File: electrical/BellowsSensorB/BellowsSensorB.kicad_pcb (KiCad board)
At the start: 2 copper layers, 32 x 20 mm, 5 parts, among them J1 I2C, U1 WF200DPZ 0.1BG S16 DT

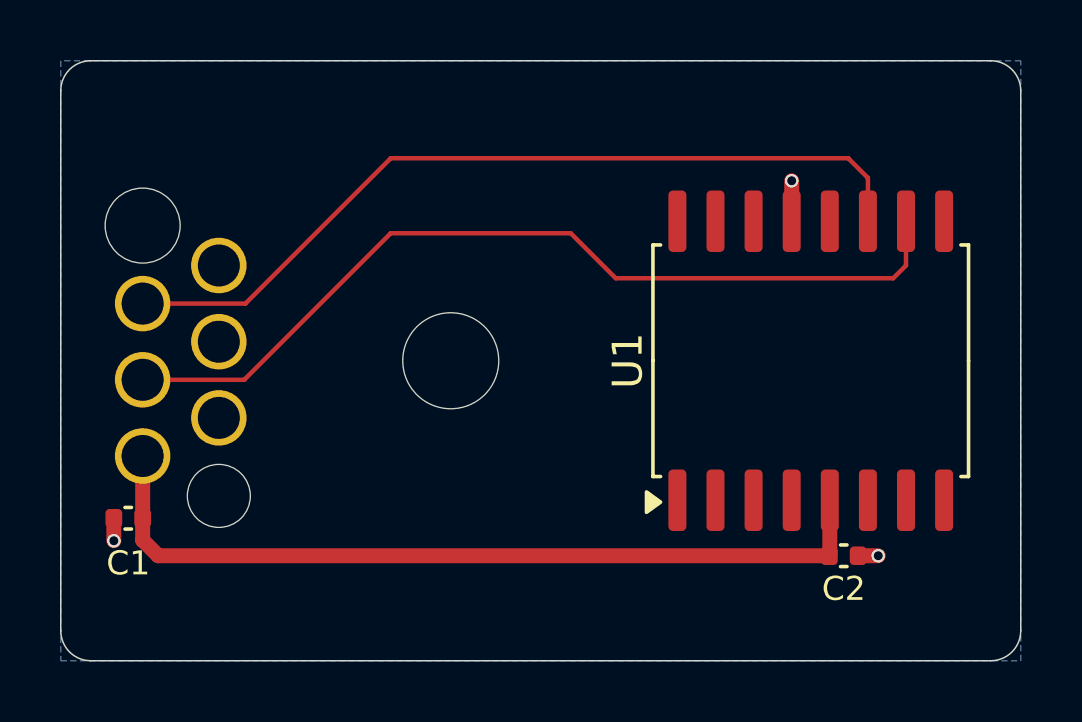
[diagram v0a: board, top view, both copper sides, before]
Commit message: Add solder bridges to BellowsSensorB
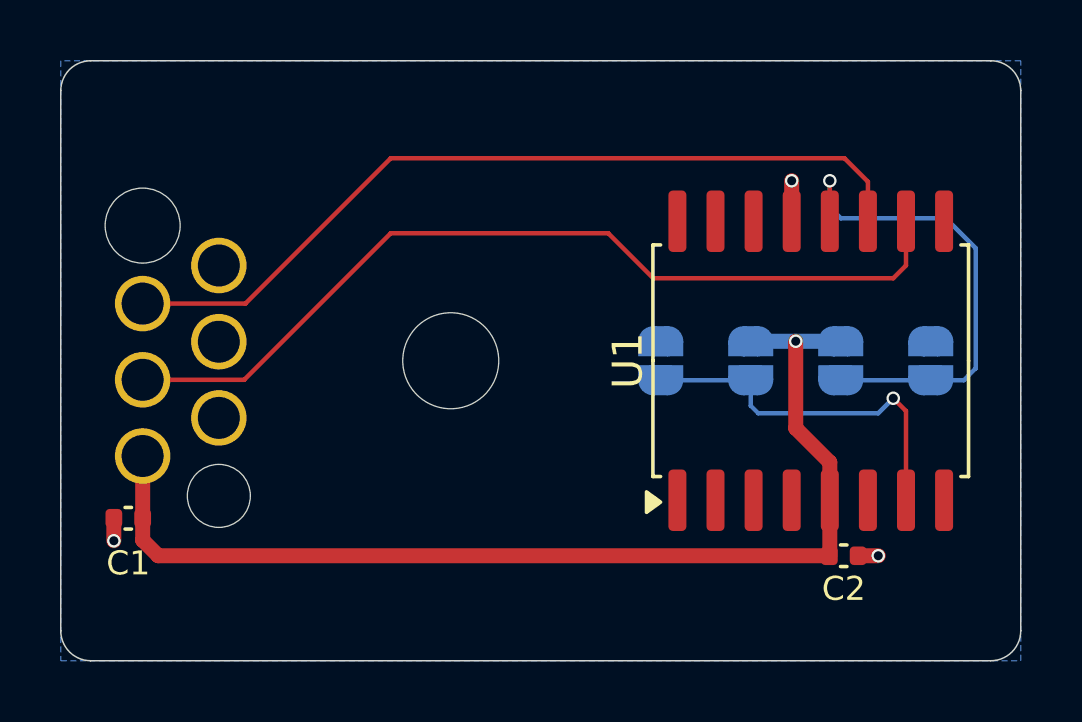
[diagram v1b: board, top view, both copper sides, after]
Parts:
- added JP1: +, Jumper:SolderJumper-2_P1.3mm_Open_RoundedPad1.0x1.5mm, B.Cu at (154.0, 104.0)
- added JP2: +, Jumper:SolderJumper-2_P1.3mm_Open_RoundedPad1.0x1.5mm, B.Cu at (151.0, 104.0)
- added JP3: -, Jumper:SolderJumper-2_P1.3mm_Open_RoundedPad1.0x1.5mm, B.Cu at (157.0, 104.0)
- added JP4: -, Jumper:SolderJumper-2_P1.3mm_Open_RoundedPad1.0x1.5mm, B.Cu at (148.0, 104.0)
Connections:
- U1 pad 12: unconnected-(U1-ADDR-Pad12) -> Net-(JP1-A)
- U1 pad 7: unconnected-(U1-CS-Pad7) -> Net-(JP2-A)
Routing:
- net Net-(JP1-A): track 0.00 -> 16.3 mm, vias 0 -> 1
- net Net-(JP2-A): track 0.00 -> 12.5 mm, vias 0 -> 1
- net +3.3V: track 27.8 -> 36.5 mm, vias 0 -> 1
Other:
- board text added: "+"
- board text added: "-"
- board text added: "ADDR"
- board text added: "CS"
